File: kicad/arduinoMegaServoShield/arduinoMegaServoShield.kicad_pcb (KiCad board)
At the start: 2 copper layers, 85.1 x 53.3 mm, 53 parts, among them J1 Screw_Terminal_01x02, M3 Motor_Servo

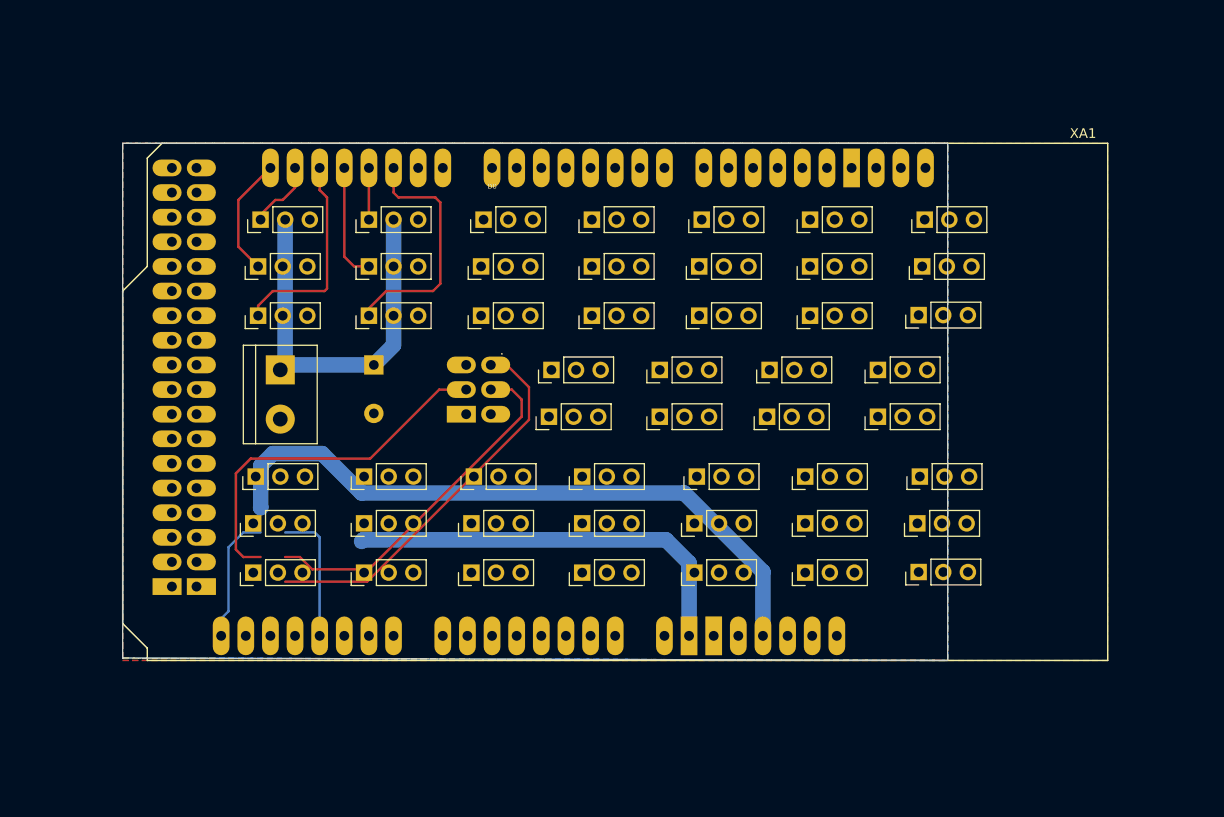
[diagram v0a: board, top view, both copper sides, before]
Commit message: added all connectors
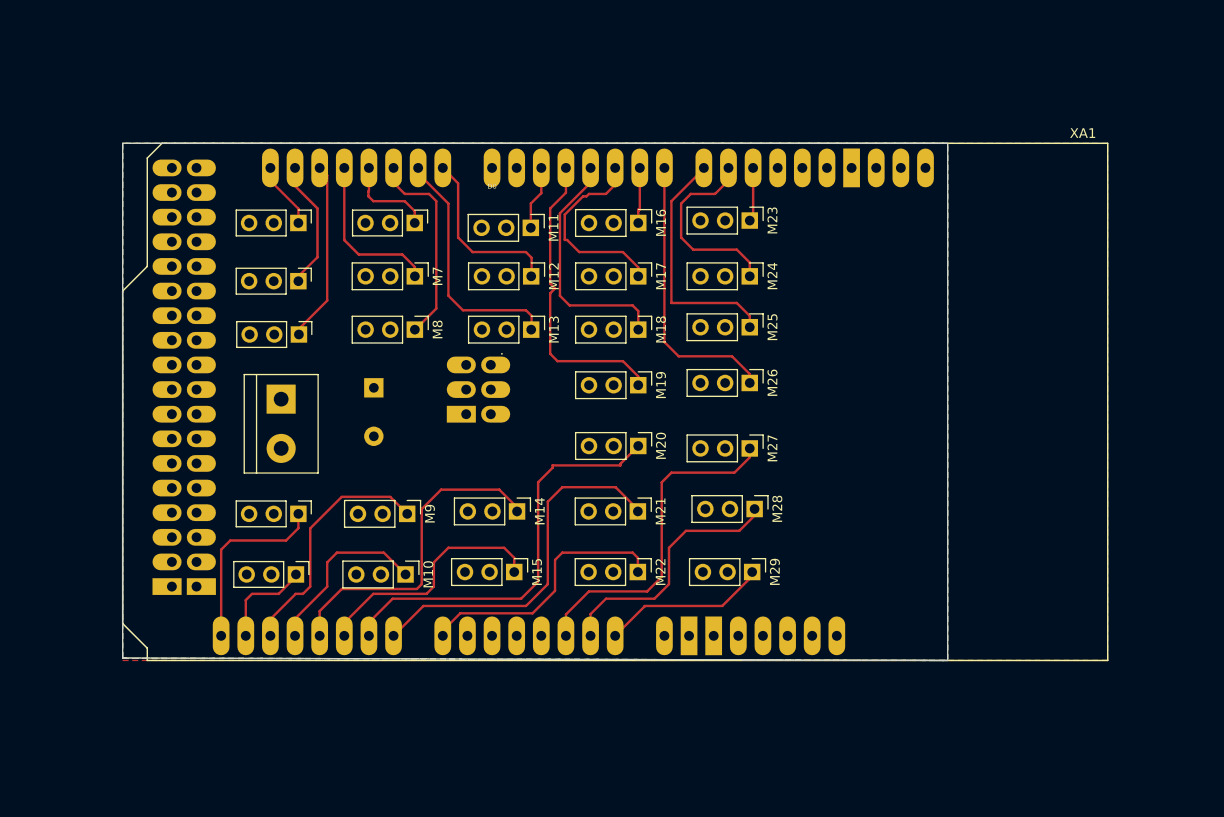
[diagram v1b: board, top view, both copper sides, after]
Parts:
- removed D16 (x5), D17 (x7), D18 (x7), D19 (x5), D21 (x9): Motor_Servo, Connector_PinHeader_2.54mm:PinHeader_1x03_P2.54mm_Vertical
- removed the M3 at (92.1, 41.2)
- removed the M3 at (85.1, 25.7)
- removed the M3 at (107.5, 35.5)
- removed the M3 at (107.6, 52.2)
- removed the M3 at (108.1, 25.7)
- removed the M3 at (69.6, 41.2)
- removed the M3 at (39.1, 52.2)
- removed the M3 at (107.5, 62.0)
- removed the M3 at (84.6, 52.2)
- removed the M3 at (62.6, 25.7)
- removed the M3 at (61.6, 52.2)
- added M10: Motor_Servo, Connector_PinHeader_2.54mm:PinHeader_1x03_P2.54mm_Vertical, F.Cu at (54.6, 62.2)
- added M11: Motor_Servo, Connector_PinHeader_2.54mm:PinHeader_1x03_P2.54mm_Vertical, F.Cu at (67.5, 26.5)
- added M12: Motor_Servo, Connector_PinHeader_2.54mm:PinHeader_1x03_P2.54mm_Vertical, F.Cu at (67.5, 31.5)
- added M13: Motor_Servo, Connector_PinHeader_2.54mm:PinHeader_1x03_P2.54mm_Vertical, F.Cu at (67.5, 37.0)
- added M14: Motor_Servo, Connector_PinHeader_2.54mm:PinHeader_1x03_P2.54mm_Vertical, F.Cu at (66.1, 55.8)
- added M15: Motor_Servo, Connector_PinHeader_2.54mm:PinHeader_1x03_P2.54mm_Vertical, F.Cu at (65.8, 62.0)
- added M16: Motor_Servo, Connector_PinHeader_2.54mm:PinHeader_1x03_P2.54mm_Vertical, F.Cu at (78.6, 26.0)
- added M17: Motor_Servo, Connector_PinHeader_2.54mm:PinHeader_1x03_P2.54mm_Vertical, F.Cu at (78.6, 31.5)
- added M18: Motor_Servo, Connector_PinHeader_2.54mm:PinHeader_1x03_P2.54mm_Vertical, F.Cu at (78.6, 37.0)
- added M19: Motor_Servo, Connector_PinHeader_2.54mm:PinHeader_1x03_P2.54mm_Vertical, F.Cu at (78.6, 42.7)
- added M20: Motor_Servo, Connector_PinHeader_2.54mm:PinHeader_1x03_P2.54mm_Vertical, F.Cu at (78.6, 49.0)
- added M21: Motor_Servo, Connector_PinHeader_2.54mm:PinHeader_1x03_P2.54mm_Vertical, F.Cu at (78.5, 55.8)
- added M22: Motor_Servo, Connector_PinHeader_2.54mm:PinHeader_1x03_P2.54mm_Vertical, F.Cu at (78.5, 62.0)
- added M23: Motor_Servo, Connector_PinHeader_2.54mm:PinHeader_1x03_P2.54mm_Vertical, F.Cu at (90.1, 25.8)
- added M24: Motor_Servo, Connector_PinHeader_2.54mm:PinHeader_1x03_P2.54mm_Vertical, F.Cu at (90.1, 31.5)
- added M25: Motor_Servo, Connector_PinHeader_2.54mm:PinHeader_1x03_P2.54mm_Vertical, F.Cu at (90.1, 36.8)
- added M26: Motor_Servo, Connector_PinHeader_2.54mm:PinHeader_1x03_P2.54mm_Vertical, F.Cu at (90.1, 42.5)
- added M27: Motor_Servo, Connector_PinHeader_2.54mm:PinHeader_1x03_P2.54mm_Vertical, F.Cu at (90.1, 49.2)
- added M28: Motor_Servo, Connector_PinHeader_2.54mm:PinHeader_1x03_P2.54mm_Vertical, F.Cu at (90.6, 55.5)
- added M29: Motor_Servo, Connector_PinHeader_2.54mm:PinHeader_1x03_P2.54mm_Vertical, F.Cu at (90.3, 62.0)
- added M7: Motor_Servo, Connector_PinHeader_2.54mm:PinHeader_1x03_P2.54mm_Vertical, F.Cu at (55.5, 31.5)
- added M8: Motor_Servo, Connector_PinHeader_2.54mm:PinHeader_1x03_P2.54mm_Vertical, F.Cu at (55.5, 37.0)
- added M9: Motor_Servo, Connector_PinHeader_2.54mm:PinHeader_1x03_P2.54mm_Vertical, F.Cu at (54.8, 56.0)
- moved M5 32.6 mm to (43.3, 62.2), turned to -90 degrees
- moved M4 21.7 mm to (43.5, 56.0), turned to -90 degrees
- moved M3 12.5 mm to (43.6, 37.5), turned to -90 degrees
- moved M1 10.4 mm to (43.5, 26.0), turned to -90 degrees
- moved M6 4.74 mm to (55.5, 26.0), turned to -90 degrees
- moved M2 4.42 mm to (43.5, 32.0), turned to -90 degrees
- moved J1 3.02 mm to (41.8, 44.2)
- moved C3 2.36 mm to (51.3, 43.0)
- renumbered D19 to M1, D21 to M2, D16 to M4, D18 to M5, D17 to M6
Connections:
- C3 pad 1: Net-(J1-Pin_1) -> +5VP
- J1 pad 1: Net-(J1-Pin_1) -> +5VP
- M1 pad 2: Net-(J1-Pin_1) -> +5VP
- M2 pad 2: Net-(J1-Pin_1) -> +5VP
- M3 pad 2: Net-(J1-Pin_1) -> +5VP
- M4 pad 2: Net-(J1-Pin_1) -> unconnected-(M4-+-Pad2)
- M4 pad 3: GND -> unconnected-(M4---Pad3)
- M5 pad 2: Net-(J1-Pin_1) -> unconnected-(M5-+-Pad2)
- M5 pad 3: GND -> unconnected-(M5---Pad3)
- M6 pad 2: Net-(J1-Pin_1) -> +5VP
- XA1 pad 3V3: +3.3V -> unconnected-(XA1-3.3V-Pad3V3)
- XA1 pad A0: unconnected-(XA1-PadA0) -> Net-(M29-PWM)
- XA1 pad A1: unconnected-(XA1-PadA1) -> Net-(M28-PWM)
- XA1 pad A10: unconnected-(XA1-PadA10) -> Net-(M15-PWM)
- XA1 pad A12: unconnected-(XA1-PadA12) -> Net-(M10-PWM)
- XA1 pad A13: unconnected-(XA1-PadA13) -> Net-(M9-PWM)
- XA1 pad A14: unconnected-(XA1-PadA14) -> Net-(M5-PWM)
- XA1 pad A15: Net-(U1-~{CSN}) -> Net-(M4-PWM)
- XA1 pad A2: unconnected-(XA1-PadA2) -> Net-(M27-PWM)
- XA1 pad A7: unconnected-(XA1-PadA7) -> Net-(M22-PWM)
- XA1 pad A8: unconnected-(XA1-PadA8) -> Net-(M21-PWM)
- XA1 pad A9: unconnected-(XA1-PadA9) -> Net-(M20-PWM)
- XA1 pad D10: unconnected-(XA1-PadD10) -> Net-(M23-PWM)
- XA1 pad D14: unconnected-(XA1-D14/TX3-PadD14) -> Net-(M12-PWM)
- XA1 pad D15: unconnected-(XA1-D15/RX3-PadD15) -> Net-(M13-PWM)
- XA1 pad D16: Net-(M4-PWM) -> Net-(M8-PWM)
- XA1 pad D18: Net-(M5-PWM) -> Net-(M7-PWM)
- XA1 pad D19: Net-(M1-PWM) -> Net-(M3-PWM)
- XA1 pad D2: unconnected-(XA1-D2_INT0-PadD2) -> Net-(M11-PWM)
- XA1 pad D20: Net-(M3-PWM) -> Net-(M2-PWM)
- XA1 pad D21: Net-(M2-PWM) -> Net-(M1-PWM)
- XA1 pad D3: unconnected-(XA1-D3_INT1-PadD3) -> Net-(M19-PWM)
- XA1 pad D4: unconnected-(XA1-PadD4) -> Net-(M18-PWM)
- XA1 pad D5: unconnected-(XA1-PadD5) -> Net-(M17-PWM)
- XA1 pad D6: unconnected-(XA1-PadD6) -> Net-(M16-PWM)
- XA1 pad D7: unconnected-(XA1-PadD7) -> Net-(M26-PWM)
- XA1 pad D8: unconnected-(XA1-PadD8) -> Net-(M25-PWM)
- XA1 pad D9: unconnected-(XA1-PadD9) -> Net-(M24-PWM)
- XA1 pad MISO: Net-(U1-MISO) -> unconnected-(XA1-SPI_MISO-PadMISO)
- XA1 pad MOSI: Net-(U1-MOSI) -> unconnected-(XA1-SPI_MOSI-PadMOSI)
- XA1 pad SCK: Net-(U1-SCK) -> unconnected-(XA1-SPI_SCK-PadSCK)
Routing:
- net +3.3V: track 68.3 -> 0.00 mm
- net Net-(M20-PWM): track 0.00 -> 42.9 mm
- net GND: track 42.4 -> 0.00 mm
- net Net-(J1-Pin_1): track 40.7 -> 0.00 mm
- net Net-(U1-MISO): track 40.3 -> 0.00 mm
- net Net-(U1-MOSI): track 38.1 -> 0.00 mm
- net Net-(M21-PWM): track 0.00 -> 37.7 mm
- net Net-(U1-SCK): track 36.8 -> 0.00 mm
- net Net-(M27-PWM): track 0.00 -> 34.5 mm
- net Net-(M19-PWM): track 0.00 -> 31.2 mm
- net Net-(M26-PWM): track 0.00 -> 29.0 mm
- net Net-(M22-PWM): track 0.00 -> 27.5 mm
- net Net-(M28-PWM): track 0.00 -> 26.2 mm
- net Net-(M15-PWM): track 0.00 -> 25.4 mm
- net Net-(M13-PWM): track 0.00 -> 25.3 mm
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- added copper zone on B.Cu, net +5VP
- added copper zone on B.Cu, net unconnected-(XA1-3.3V-Pad3V3)
- removed copper zone on B.Cu, net +3.3V

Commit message: improved layout
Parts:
- removed M22, M24, M3: Motor_Servo, Connector_PinHeader_2.54mm:PinHeader_1x03_P2.54mm_Vertical
- added M30: Motor_Servo, Connector_PinHeader_2.54mm:PinHeader_1x03_P2.54mm_Vertical, F.Cu at (38.9, 33.8)
- added M31: Motor_Servo, Connector_PinHeader_2.54mm:PinHeader_1x03_P2.54mm_Vertical, F.Cu at (38.2, 40.0)
- added M34: Motor_Servo, Connector_PinHeader_2.54mm:PinHeader_1x03_P2.54mm_Vertical, F.Cu at (60.7, 50.0)
- added M35: Motor_Servo, Connector_PinHeader_2.54mm:PinHeader_1x03_P2.54mm_Vertical, F.Cu at (105.4, 67.0)
- added M36: Motor_Servo, Connector_PinHeader_2.54mm:PinHeader_1x03_P2.54mm_Vertical, F.Cu at (105.7, 60.5)
- added M37: Motor_Servo, Connector_PinHeader_2.54mm:PinHeader_1x03_P2.54mm_Vertical, F.Cu at (95.5, 42.2)
- added M38: Motor_Servo, Connector_PinHeader_2.54mm:PinHeader_1x03_P2.54mm_Vertical, F.Cu at (95.7, 37.0)
- added M39: Motor_Servo, Connector_PinHeader_2.54mm:PinHeader_1x03_P2.54mm_Vertical, F.Cu at (96.2, 31.0)
- added M40: Motor_Servo, Connector_PinHeader_2.54mm:PinHeader_1x03_P2.54mm_Vertical, F.Cu at (96.0, 25.5)
- added M41: Motor_Servo, Connector_PinHeader_2.54mm:PinHeader_1x03_P2.54mm_Vertical, F.Cu at (100.9, 52.2)
- moved J1 79.8 mm to (121.2, 50.6), turned to 90 degrees
- moved C3 61.1 mm to (112.0, 50.2), turned to 90 degrees
- moved M23 23.8 mm to (72.9, 42.2), turned to 90 degrees
- moved M26 23.8 mm to (72.7, 26.2), turned to 90 degrees
- moved M27 21.8 mm to (72.9, 62.8), turned to 90 degrees
- moved M13 21.4 mm to (49.2, 48.0), turned to 90 degrees
- moved M29 21.4 mm to (72.7, 50.0), turned to 90 degrees
- moved M19 18.4 mm to (84.4, 25.3), turned to 90 degrees
- moved M28 18.2 mm to (72.4, 56.5), turned to 90 degrees
- moved M2 18.1 mm to (38.8, 49.5), turned to 90 degrees
- moved M14 17.9 mm to (49.4, 62.2), turned to 90 degrees
- moved M25 17.4 mm to (72.9, 33.8), turned to 90 degrees
- moved M15 17.2 mm to (49.7, 56.0), turned to 90 degrees
- moved M16 17.0 mm to (84.4, 42.0), turned to 90 degrees
- moved M20 15.2 mm to (84.4, 63.0), turned to 90 degrees
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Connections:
- M1 pad 2: +5VP -> unconnected-(M1-+-Pad2)
- M1 pad 3: GND -> unconnected-(M1---Pad3)
- M11 pad 2: +5VP -> unconnected-(M11-+-Pad2)
- M11 pad 3: GND -> unconnected-(M11---Pad3)
- M12 pad 2: +5VP -> unconnected-(M12-+-Pad2)
- M12 pad 3: GND -> unconnected-(M12---Pad3)
- M13 pad 2: +5VP -> unconnected-(M13-+-Pad2)
- M13 pad 3: GND -> unconnected-(M13---Pad3)
- M15 pad 1: Net-(M15-PWM) -> unconnected-(M15-PWM-Pad1)
- M16 pad 2: +5VP -> unconnected-(M16-+-Pad2)
- M16 pad 3: GND -> unconnected-(M16---Pad3)
- M17 pad 2: +5VP -> unconnected-(M17-+-Pad2)
- M17 pad 3: GND -> unconnected-(M17---Pad3)
- M18 pad 2: +5VP -> unconnected-(M18-+-Pad2)
- M18 pad 3: GND -> unconnected-(M18---Pad3)
- M19 pad 3: GND -> unconnected-(M19---Pad3)
- M23 pad 2: +5VP -> unconnected-(M23-+-Pad2)
- M23 pad 3: GND -> unconnected-(M23---Pad3)
- M25 pad 2: +5VP -> unconnected-(M25-+-Pad2)
- M25 pad 3: GND -> unconnected-(M25---Pad3)
- M26 pad 2: +5VP -> unconnected-(M26-+-Pad2)
- M26 pad 3: GND -> unconnected-(M26---Pad3)
- M27 pad 2: +5VP -> unconnected-(M27-+-Pad2)
- M27 pad 3: GND -> unconnected-(M27---Pad3)
- M28 pad 2: +5VP -> unconnected-(M28-+-Pad2)
- M28 pad 3: GND -> unconnected-(M28---Pad3)
- M29 pad 2: +5VP -> unconnected-(M29-+-Pad2)
- M29 pad 3: GND -> unconnected-(M29---Pad3)
- M4 pad 2: unconnected-(M4-+-Pad2) -> +5VP
- M4 pad 3: unconnected-(M4---Pad3) -> GND
- M6 pad 2: +5VP -> unconnected-(M6-+-Pad2)
- M6 pad 3: GND -> unconnected-(M6---Pad3)
- M7 pad 2: +5VP -> unconnected-(M7-+-Pad2)
- M7 pad 3: GND -> unconnected-(M7---Pad3)
- M8 pad 2: +5VP -> unconnected-(M8-+-Pad2)
- M8 pad 3: GND -> unconnected-(M8---Pad3)
- XA1 pad A0: Net-(M29-PWM) -> Net-(M20-PWM)
- XA1 pad A1: Net-(M28-PWM) -> Net-(M21-PWM)
- XA1 pad A10: Net-(M15-PWM) -> Net-(M14-PWM)
- XA1 pad A11: Net-(M14-PWM) -> unconnected-(XA1-PadA11)
- XA1 pad A12: Net-(M10-PWM) -> unconnected-(XA1-PadA12)
- XA1 pad A13: Net-(M9-PWM) -> unconnected-(XA1-PadA13)
- XA1 pad A14: Net-(M5-PWM) -> unconnected-(XA1-PadA14)
- XA1 pad A15: Net-(M4-PWM) -> Net-(M5-PWM)
- XA1 pad A3: unconnected-(XA1-PadA3) -> Net-(M28-PWM)
- XA1 pad A4: unconnected-(XA1-PadA4) -> Net-(M29-PWM)
- XA1 pad A5: unconnected-(XA1-PadA5) -> Net-(M23-PWM)
- XA1 pad A6: unconnected-(XA1-PadA6) -> Net-(M9-PWM)
- XA1 pad A7: Net-(M22-PWM) -> Net-(M10-PWM)
- XA1 pad A8: Net-(M21-PWM) -> Net-(M34-PWM)
- XA1 pad A9: Net-(M20-PWM) -> Net-(M13-PWM)
- XA1 pad D10: Net-(M23-PWM) -> Net-(M40-PWM)
- XA1 pad D11: unconnected-(XA1-PadD11) -> Net-(M39-PWM)
- XA1 pad D12: unconnected-(XA1-PadD12) -> Net-(M38-PWM)
- XA1 pad D13: unconnected-(XA1-PadD13) -> Net-(M37-PWM)
- XA1 pad D14: Net-(M12-PWM) -> unconnected-(XA1-D14/TX3-PadD14)
- XA1 pad D15: Net-(M13-PWM) -> unconnected-(XA1-D15/RX3-PadD15)
- XA1 pad D16: Net-(M8-PWM) -> unconnected-(XA1-D16/TX2-PadD16)
- XA1 pad D17: Net-(M6-PWM) -> unconnected-(XA1-D17/RX2-PadD17)
- XA1 pad D18: Net-(M7-PWM) -> unconnected-(XA1-D18/TX1-PadD18)
- XA1 pad D19: Net-(M3-PWM) -> unconnected-(XA1-D19/RX1-PadD19)
- XA1 pad D2: Net-(M11-PWM) -> unconnected-(XA1-D2_INT0-PadD2)
- XA1 pad D20: Net-(M2-PWM) -> Net-(M26-PWM)
- XA1 pad D21: Net-(M1-PWM) -> Net-(M11-PWM)
- XA1 pad D22: unconnected-(XA1-PadD22) -> Net-(M1-PWM)
- XA1 pad D24: unconnected-(XA1-PadD24) -> Net-(M6-PWM)
- XA1 pad D28: unconnected-(XA1-PadD28) -> Net-(M25-PWM)
- XA1 pad D3: Net-(M19-PWM) -> unconnected-(XA1-D3_INT1-PadD3)
- XA1 pad D30: unconnected-(XA1-PadD30) -> Net-(M12-PWM)
- XA1 pad D32: unconnected-(XA1-PadD32) -> Net-(M7-PWM)
- XA1 pad D34: unconnected-(XA1-PadD34) -> Net-(M30-PWM)
- XA1 pad D36: unconnected-(XA1-PadD36) -> Net-(M16-PWM)
- XA1 pad D38: unconnected-(XA1-PadD38) -> Net-(M31-PWM)
- XA1 pad D4: Net-(M18-PWM) -> Net-(M17-PWM)
- XA1 pad D40: unconnected-(XA1-PadD40) -> Net-(M8-PWM)
- XA1 pad D46: unconnected-(XA1-PadD46) -> Net-(M2-PWM)
- XA1 pad D48: unconnected-(XA1-PadD48) -> Net-(M4-PWM)
- XA1 pad D5: Net-(M17-PWM) -> Net-(M18-PWM)
- XA1 pad D6: Net-(M16-PWM) -> Net-(M19-PWM)
- XA1 pad D7: Net-(M26-PWM) -> Net-(M35-PWM)
- XA1 pad D8: Net-(M25-PWM) -> Net-(M36-PWM)
- XA1 pad GND4: GND -> unconnected-(XA1-SPI_GND-PadGND4)
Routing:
- net Net-(M35-PWM): track 0.00 -> 61.8 mm
- net Net-(M36-PWM): track 0.00 -> 53.0 mm
- net Net-(M16-PWM): track 5.92 -> 53.4 mm
- net Net-(M37-PWM): track 0.00 -> 34.3 mm
- net Net-(M20-PWM): track 42.9 -> 11.5 mm
- net Net-(M38-PWM): track 0.00 -> 30.8 mm
- net Net-(M27-PWM): track 34.5 -> 6.58 mm
- net Net-(M22-PWM): track 27.5 -> 0.00 mm
- net Net-(M14-PWM): track 33.8 -> 6.82 mm
- net Net-(M39-PWM): track 0.00 -> 25.7 mm
- net Net-(M15-PWM): track 25.4 -> 0.00 mm
- net Net-(M23-PWM): track 5.57 -> 29.2 mm
- net Net-(M34-PWM): track 0.00 -> 22.7 mm
- net Net-(M19-PWM): track 31.2 -> 8.86 mm
- net Net-(M41-PWM): track 20.2 -> 40.7 mm
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- removed copper zone on B.Cu, net (none)
- removed copper zone on B.Cu, net unconnected-(XA1-3.3V-Pad3V3)
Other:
- board size 85.1 x 53.3 mm -> 101.6 x 53.4 mm

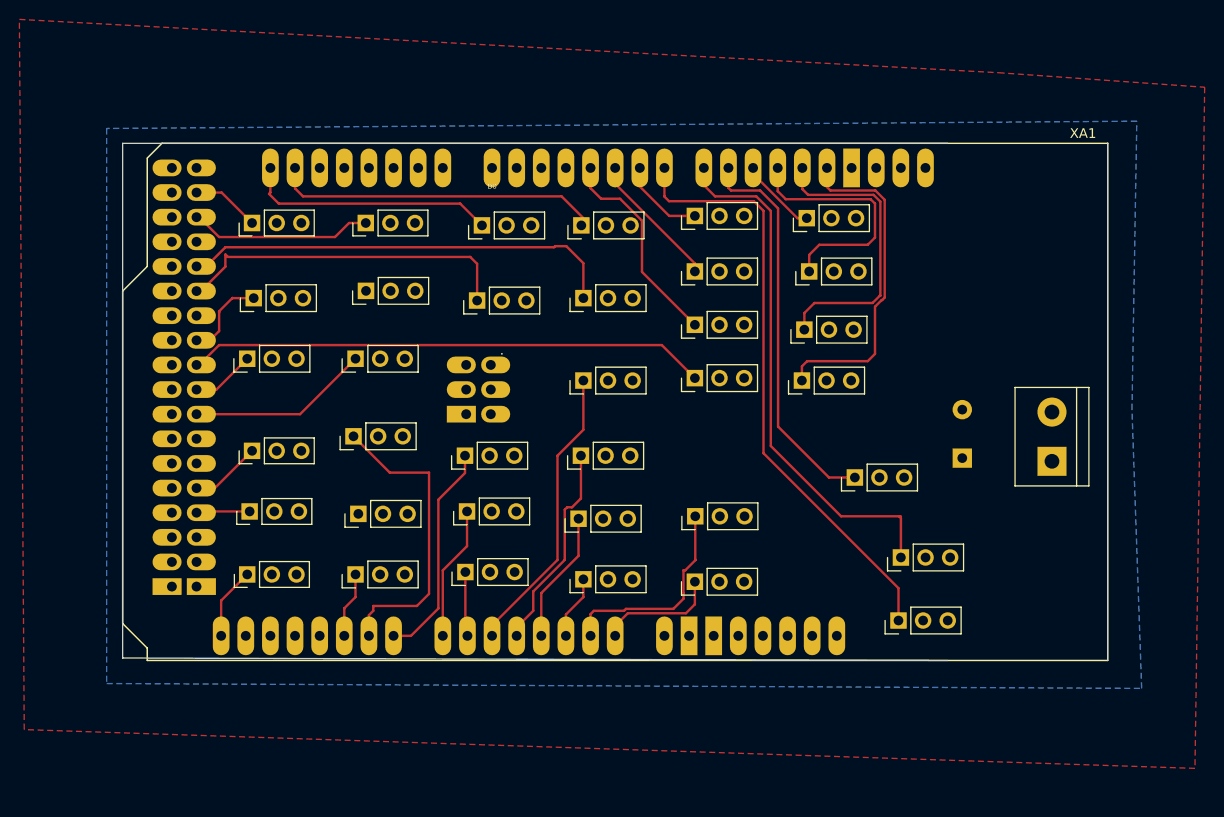
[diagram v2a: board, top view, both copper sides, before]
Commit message: added art criticism section
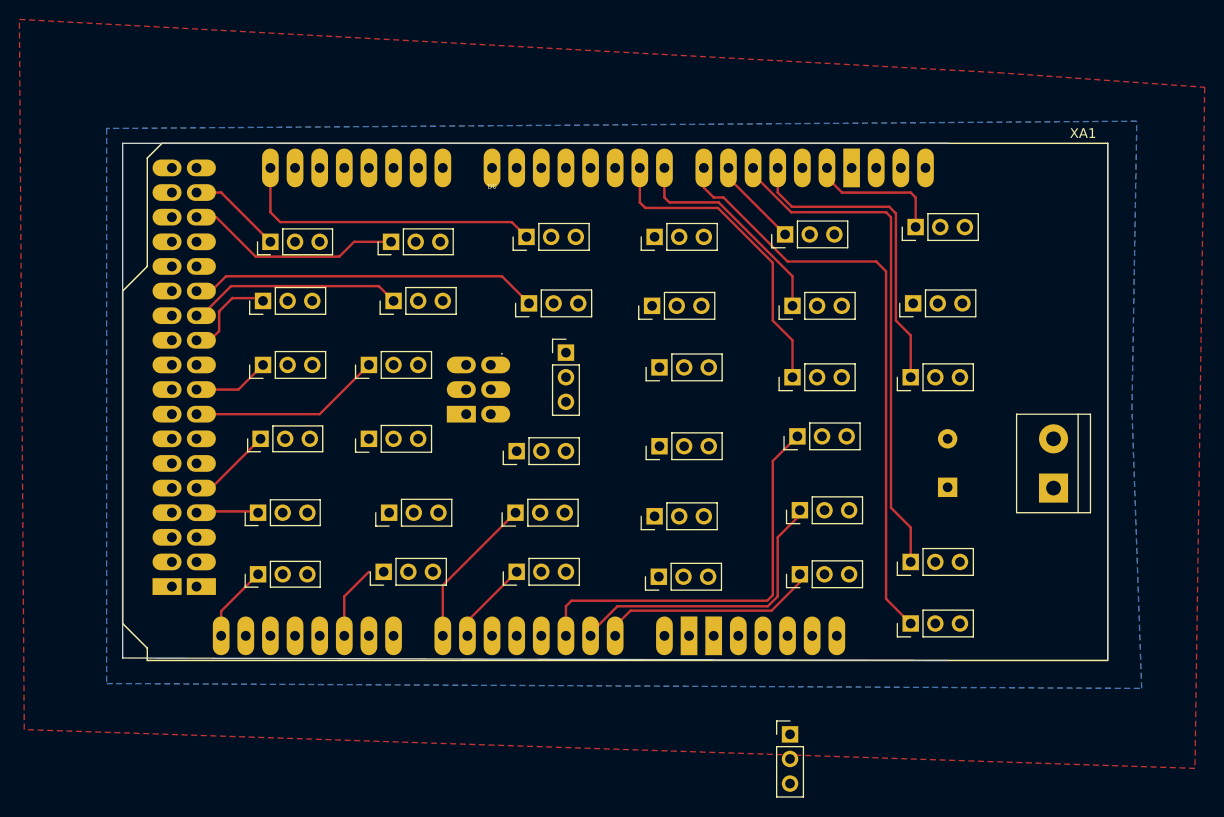
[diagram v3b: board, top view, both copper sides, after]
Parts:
- moved M41 27.3 mm to (94.2, 78.7), turned to 0 degrees
- moved M27 26.5 mm to (95.0, 48.0)
- moved M29 23.3 mm to (95.2, 55.6)
- moved M37 20.0 mm to (95.2, 62.2)
- moved M28 17.2 mm to (71.1, 39.4), turned to 0 degrees
- moved M38 12.0 mm to (106.7, 41.9)
- moved M17 11.4 mm to (94.5, 41.9)
- moved M40 11.3 mm to (107.2, 26.4)
- moved M39 11.2 mm to (106.9, 34.3)
- moved M18 10.7 mm to (94.5, 34.5)
- moved M19 9.50 mm to (93.7, 27.2)
- moved M23 7.97 mm to (80.8, 40.9)
- moved M16 7.91 mm to (80.8, 49.0)
- moved M26 7.65 mm to (80.3, 27.4)
- moved M25 7.13 mm to (80.0, 34.5)
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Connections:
- M20 pad 1: Net-(M20-PWM) -> unconnected-(M20-PWM-Pad1)
- M21 pad 1: Net-(M21-PWM) -> unconnected-(M21-PWM-Pad1)
- M25 pad 1: Net-(M25-PWM) -> unconnected-(M25-PWM-Pad1)
- M26 pad 1: Net-(M26-PWM) -> unconnected-(M26-PWM-Pad1)
- M39 pad 1: Net-(M39-PWM) -> unconnected-(M39-PWM-Pad1)
- M41 pad 1: Net-(M41-PWM) -> unconnected-(M41-PWM-Pad1)
- XA1 pad A0: Net-(M20-PWM) -> Net-(M37-PWM)
- XA1 pad A1: Net-(M21-PWM) -> Net-(M29-PWM)
- XA1 pad A4: Net-(M29-PWM) -> unconnected-(XA1-PadA4)
- XA1 pad D10: Net-(M40-PWM) -> Net-(M36-PWM)
- XA1 pad D11: Net-(M39-PWM) -> Net-(M38-PWM)
- XA1 pad D12: Net-(M38-PWM) -> unconnected-(XA1-PadD12)
- XA1 pad D13: Net-(M37-PWM) -> Net-(M40-PWM)
- XA1 pad D20: Net-(M26-PWM) -> unconnected-(XA1-D20/SDA-PadD20)
- XA1 pad D28: Net-(M25-PWM) -> unconnected-(XA1-PadD28)
- XA1 pad D4: Net-(M17-PWM) -> unconnected-(XA1-PadD4)
- XA1 pad D5: Net-(M18-PWM) -> unconnected-(XA1-PadD5)
- XA1 pad D6: Net-(M19-PWM) -> Net-(M17-PWM)
- XA1 pad D7: Net-(M35-PWM) -> Net-(M18-PWM)
- XA1 pad D8: Net-(M36-PWM) -> Net-(M35-PWM)
- XA1 pad D9: Net-(M41-PWM) -> Net-(M19-PWM)
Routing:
- net Net-(M16-PWM): track 53.4 -> 0.00 mm
- net Net-(M25-PWM): track 44.1 -> 0.00 mm
- net Net-(M41-PWM): track 40.7 -> 0.00 mm
- net Net-(M27-PWM): track 6.58 -> 42.3 mm
- net Net-(M26-PWM): track 33.1 -> 0.00 mm
- net Net-(M13-PWM): track 31.4 -> 0.00 mm
- net Net-(M23-PWM): track 29.2 -> 0.00 mm
- net Net-(M39-PWM): track 25.7 -> 0.00 mm
- net Net-(M34-PWM): track 22.7 -> 0.00 mm
- net Net-(M7-PWM): track 0.00 -> 22.2 mm
- net Net-(M21-PWM): track 21.6 -> 0.00 mm
- net Net-(M28-PWM): track 13.7 -> 0.00 mm
- net Net-(M37-PWM): track 34.3 -> 22.8 mm
- net Net-(M20-PWM): track 11.5 -> 0.00 mm
- net Net-(M17-PWM): track 21.8 -> 32.5 mm
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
